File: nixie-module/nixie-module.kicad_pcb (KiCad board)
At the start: 2 copper layers, 28.2 x 43.8 mm, 5 parts, among them P1 CONN_02X05, U1 74141

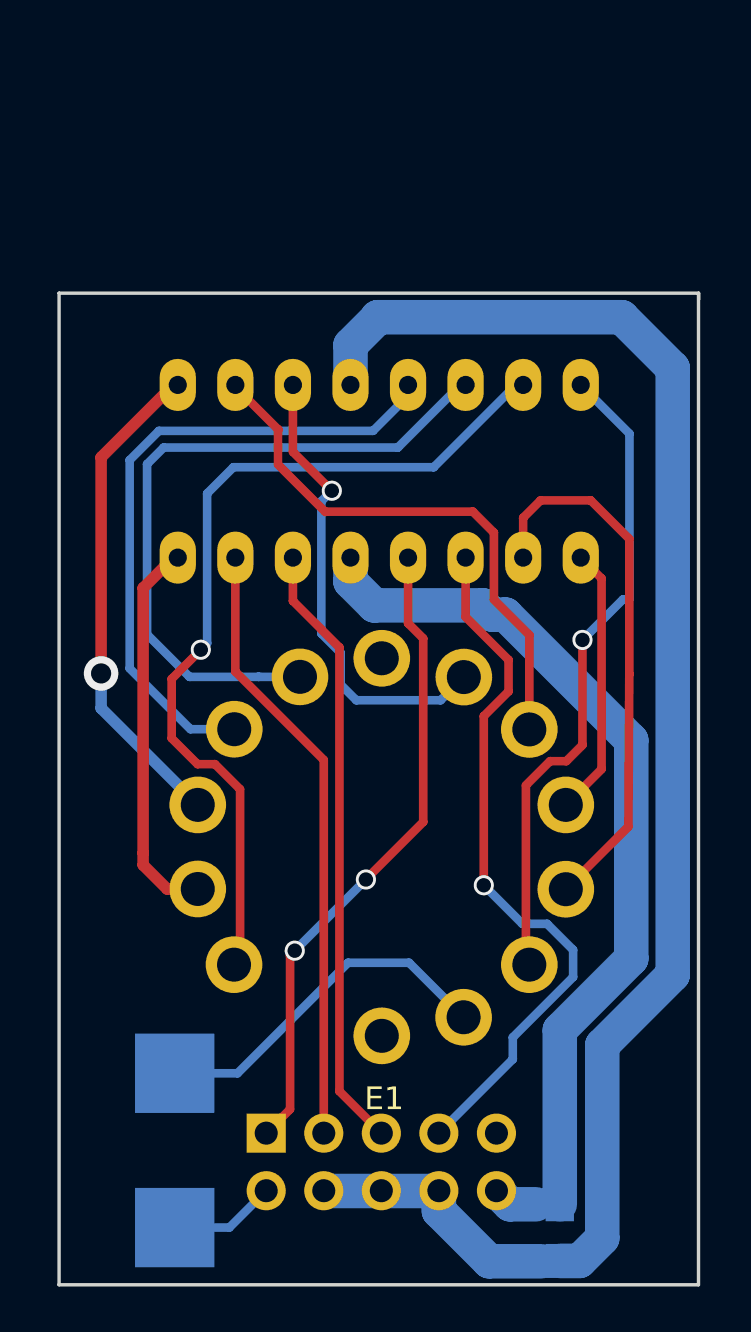
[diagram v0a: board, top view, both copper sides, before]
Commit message: Reguly DRC; wymiary plytki
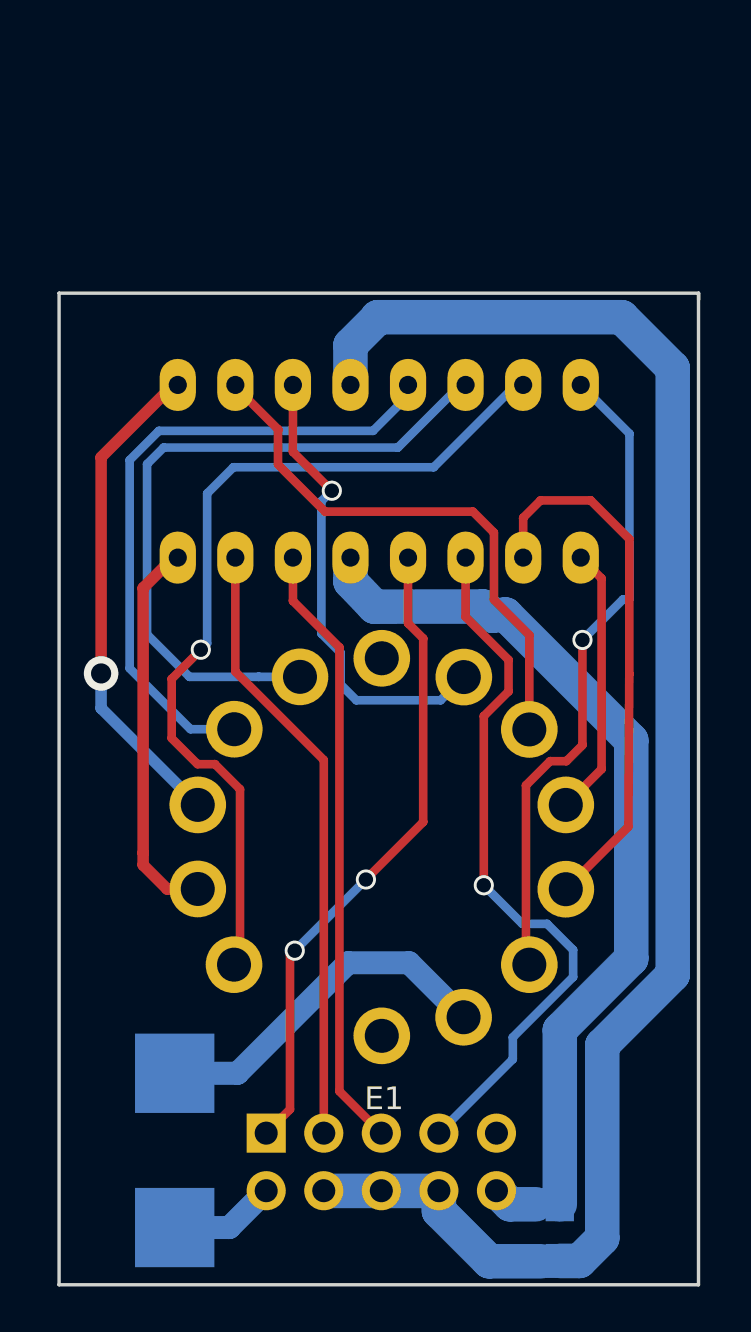
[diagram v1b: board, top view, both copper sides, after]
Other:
- net class HV: clearance 0.8128 -> 0.7874

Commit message: Odwrocenie numeracji pinow w zlaczu od modulu NIXIE
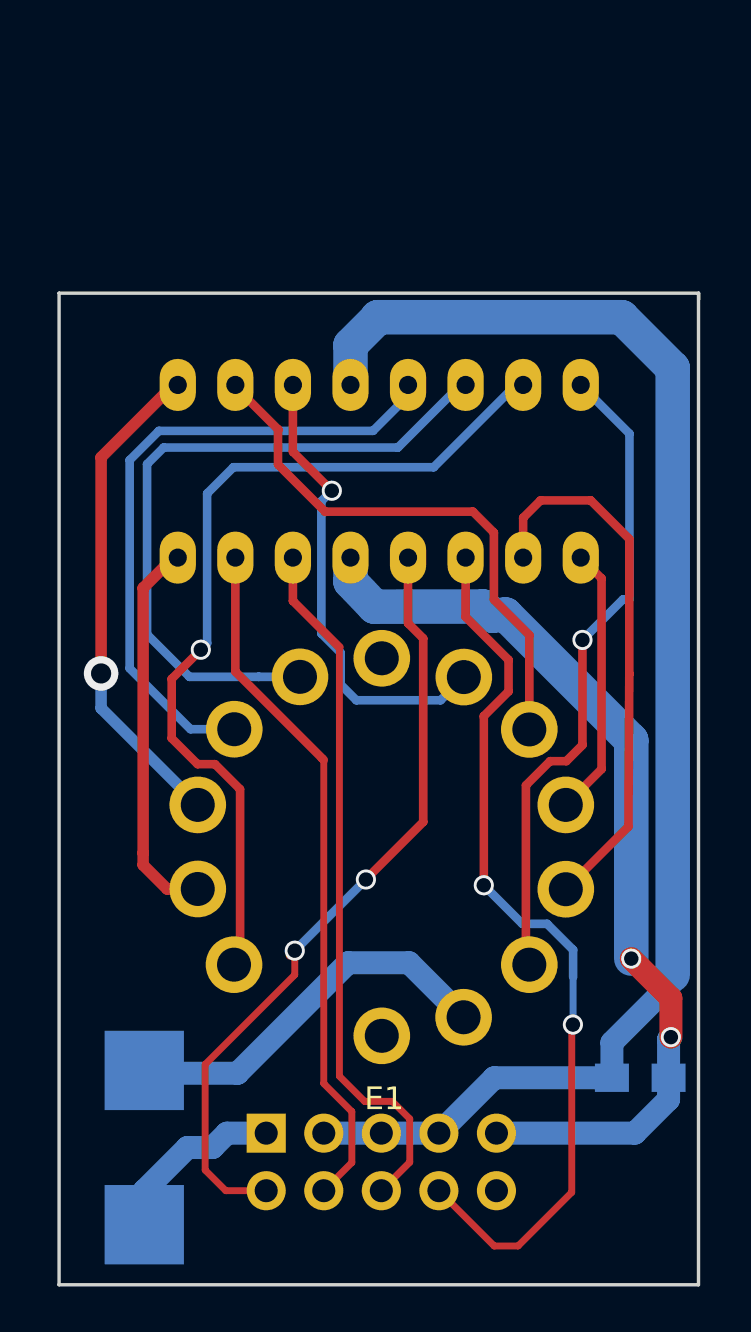
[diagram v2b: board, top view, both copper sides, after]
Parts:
- P1: footprint Pin_Headers:Pin_Header_Angled_2x05 -> nixie-module-footprint:Pin_Header_Angled_2x05
- moved C1 7.70 mm to (158.3, 119.1), turned to 180 degrees
- moved R1 1.35 mm to (136.4, 122.2)
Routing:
- net GND: track 71.7 -> 63.6 mm
- net /A: track 31.4 -> 39.4 mm, vias 1 -> 2
- net /D: track 28.5 -> 34.7 mm
- net /B: track 27.0 -> 31.3 mm
- net /C: track 27.0 -> 30.6 mm
- net Net-(P1-Pad2): track 4.71 -> 7.93 mm
- net VCC: vias 0 -> 2

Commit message: Poprawienie rozmiarow modulu NIXIE - lampa kolidowalaby z lutami od 74141 i listwy
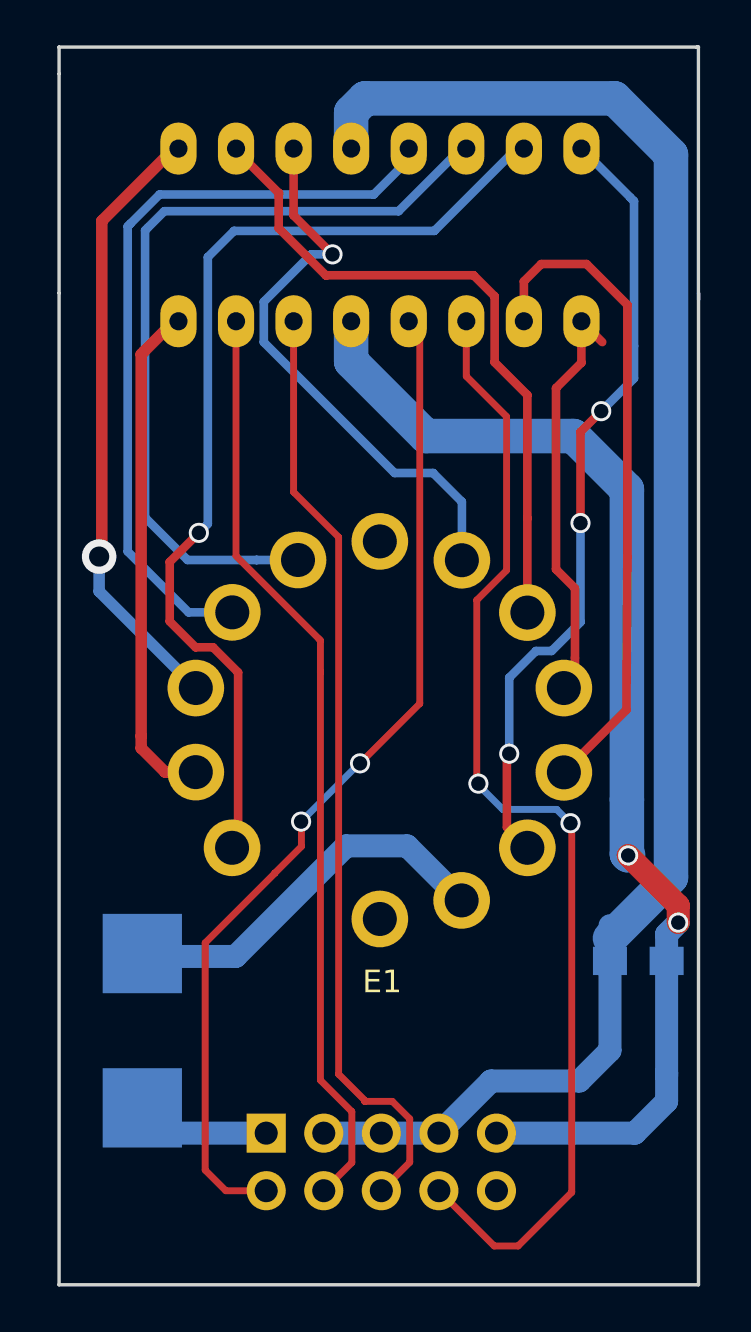
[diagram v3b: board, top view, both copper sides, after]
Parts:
- moved U1 10.4 mm to (155.7, 85.7)
- moved C1 5.16 mm to (158.2, 114.0)
- moved E1 5.16 mm to (146.8, 103.8)
- moved R1 5.16 mm to (136.3, 117.0)
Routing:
- net VCC: track 42.1 -> 53.5 mm
- net /A: track 39.4 -> 50.8 mm
- net /C: track 30.6 -> 41.1 mm
- net /B: track 31.3 -> 41.7 mm
- net /D: track 34.7 -> 44.7 mm
- net GND: track 63.6 -> 72.5 mm
- net Net-(E1-Pad5): track 11.9 -> 19.2 mm
- net Net-(E1-Pad3): track 29.0 -> 35.1 mm, vias 1 -> 3
- net Net-(E1-Pad9): track 30.6 -> 35.9 mm
- net Net-(E1-Pad12): track 17.2 -> 22.5 mm
- net Net-(E1-Pad13): track 39.2 -> 44.5 mm
- net Net-(E1-Pad11): track 21.8 -> 27.2 mm
- net Net-(E1-Pad10): track 28.9 -> 34.2 mm
- net Net-(E1-Pad6): track 24.5 -> 29.7 mm
- net Net-(E1-Pad4): track 24.6 -> 29.7 mm
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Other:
- board size 28.2 x 43.8 mm -> 28.2 x 54.6 mm

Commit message: Modyfikacja sciezek modulu NIXIE
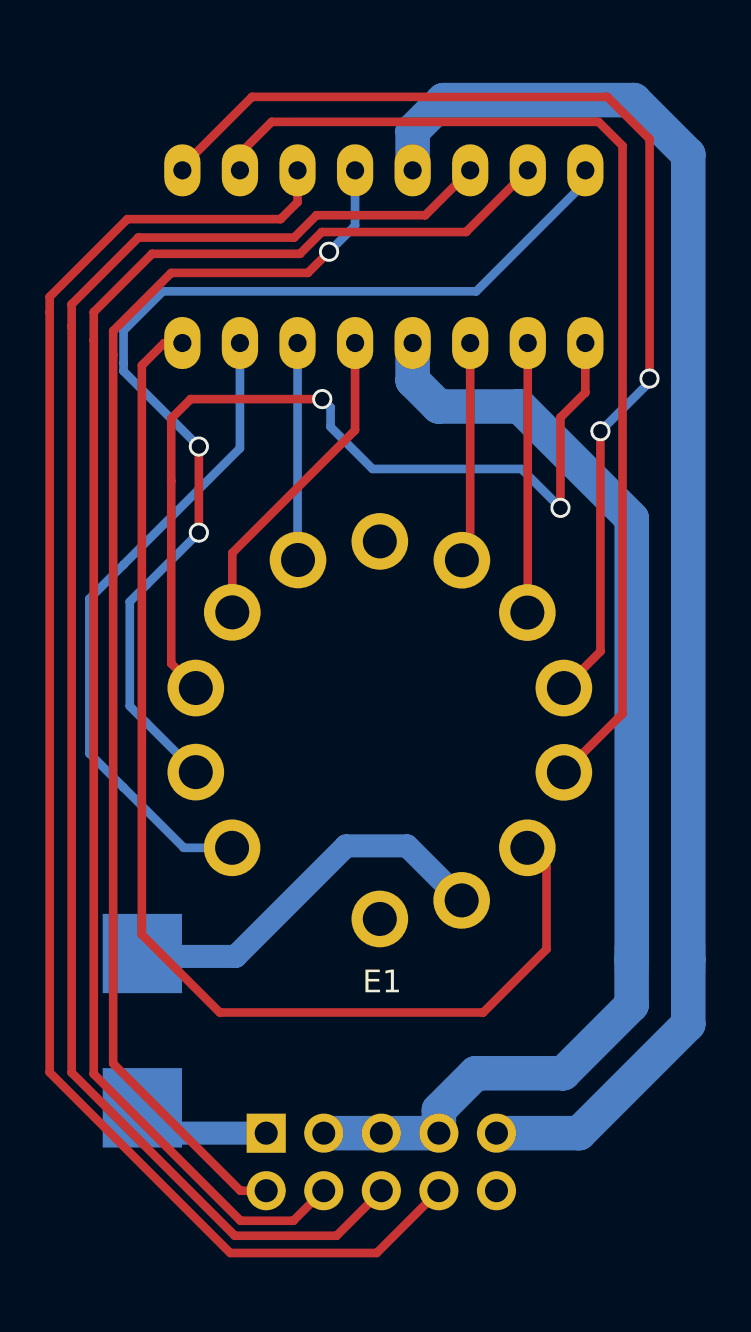
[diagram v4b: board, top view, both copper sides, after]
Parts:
- moved U1 18.8 mm to (138.1, 79.1), turned to 270 degrees
- moved C1 0.96 mm to (159.2, 113.9)
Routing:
- net Net-(E1-Pad5): track 19.2 -> 50.0 mm, vias 0 -> 2
- net /B: track 41.7 -> 71.4 mm
- net /C: track 41.1 -> 68.7 mm
- net Net-(E1-Pad9): track 35.9 -> 9.58 mm
- net Net-(E1-Pad12): track 22.5 -> 47.2 mm, vias 0 -> 2
- net GND: track 72.5 -> 51.8 mm
- net Net-(E1-Pad10): track 34.2 -> 14.1 mm
- net /A: track 50.8 -> 69.9 mm, vias 2 -> 0
- net Net-(E1-Pad6): track 29.7 -> 11.9 mm
- net Net-(E1-Pad4): track 29.7 -> 47.4 mm
- net Net-(E1-Pad3): track 35.1 -> 52.8 mm, vias 3 -> 0
- net Net-(E1-Pad7): track 25.3 -> 9.74 mm, vias 1 -> 0
- net Net-(E1-Pad13): track 44.5 -> 29.7 mm, vias 1 -> 0
- net Net-(E1-Pad11): track 27.2 -> 40.1 mm, vias 1 -> 2
- net /D: track 44.7 -> 56.4 mm, vias 2 -> 1
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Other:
- board outline removed
